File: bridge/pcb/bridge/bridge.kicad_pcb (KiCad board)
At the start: 2 copper layers, 108 x 80 mm, 45 parts, among them J1 Screw_Terminal_01x06, J2 Screw_Terminal_01x06, J3 Screw_Terminal_01x06, J4 Conn_01x23, J5 Conn_01x04, J6 Conn_01x02, J7 Conn_01x03, J8 Conn_01x02, J9 MCU_Test_Point, SW1 SW_SPST, SW2 SW_SPST, SW3 SW_SPST, SW4 SW_SPST, SW5 SW_SPST, U1 L293, U2 J104D2C12VDC.20S, U4 ATmega328P-P, U5 L7805, U6 MCP4901

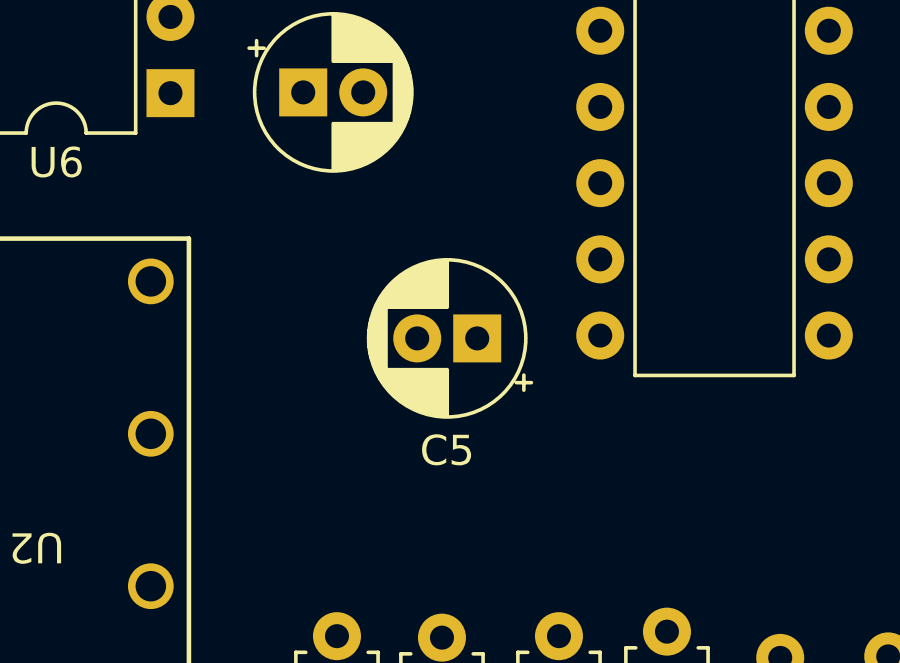
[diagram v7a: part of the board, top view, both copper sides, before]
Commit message: Added a version marker and credits to PCB
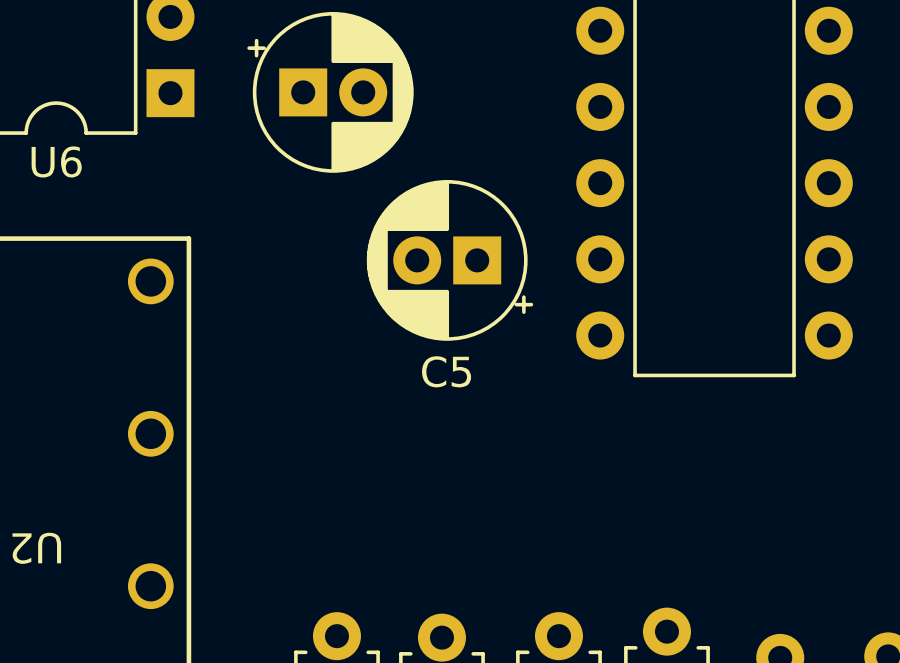
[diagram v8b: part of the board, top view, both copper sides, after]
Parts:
- moved C5 2.60 mm to (101.8, 80.0)
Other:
- board text added: "Designed 2023-2024 by Roman Rice Bridge PCB v0.3 More info at: https://github.com/Roman-Rice-Engineering/auto-golf-cart"
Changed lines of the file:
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@@
   )
   (footprint "Capacitor_THT:CP_Radial_D5.0mm_P2.00mm" (layer "F.Cu")
-    (at 101.8 82.6 180)
+    (at 101.8 80 180)
     (descr "CP, Radial series, Radial, pin pitch=2.00mm, , diameter=5mm, Electrolytic Capacitor")
     (tags "CP Radial series Radial pin pitch 2.00mm  diameter 5mm Electrolytic Capacitor")
@@
   (gr_arc (start 64 121) (mid 63.292893 120.707107) (end 63 120)
     (stroke (width 0.1) (type default)) (layer "Edge.Cuts"))
+  (gr_text "Designed 2023-2024 by Roman Rice\nBridge PCB v0.3\nMore info at:\nhttps://github.com/Roman-Rice-Engineering/auto-golf-cart" (at 146 118) (layer "B.SilkS")
+    (effects (font (size 1 1) (thickness 0.15)) (justify left bottom mirror))
+  )
   (gr_text "TX" (at 167.25 74.26) (layer "F.SilkS")
     (effects (font (size 1 1) (thickness 0.15)) (justify left bottom))
